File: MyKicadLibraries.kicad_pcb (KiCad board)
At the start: 2 copper layers, 168.6 x 98.9 mm, 27 parts, among them J1 Conn_01x08, J10 RCJ-22, J2 Conn_01x08, J3 POGO Pins, J4 c8-inlet, J5 FTDI, J6 Micro_SD_Card, J7 Conn_01x04, J8 Conn_02x04_Counter_Clockwise, J9 Conn_01x04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

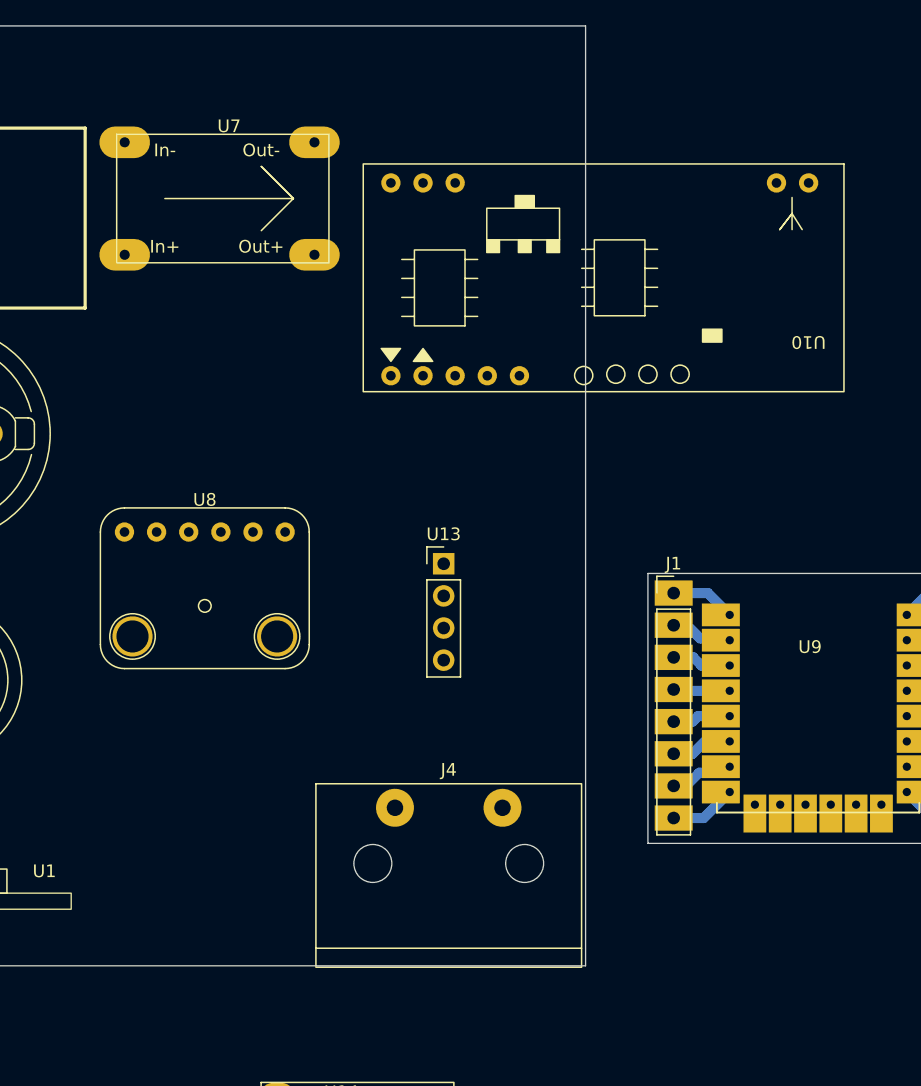
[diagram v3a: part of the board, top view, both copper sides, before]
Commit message: Add midi connector
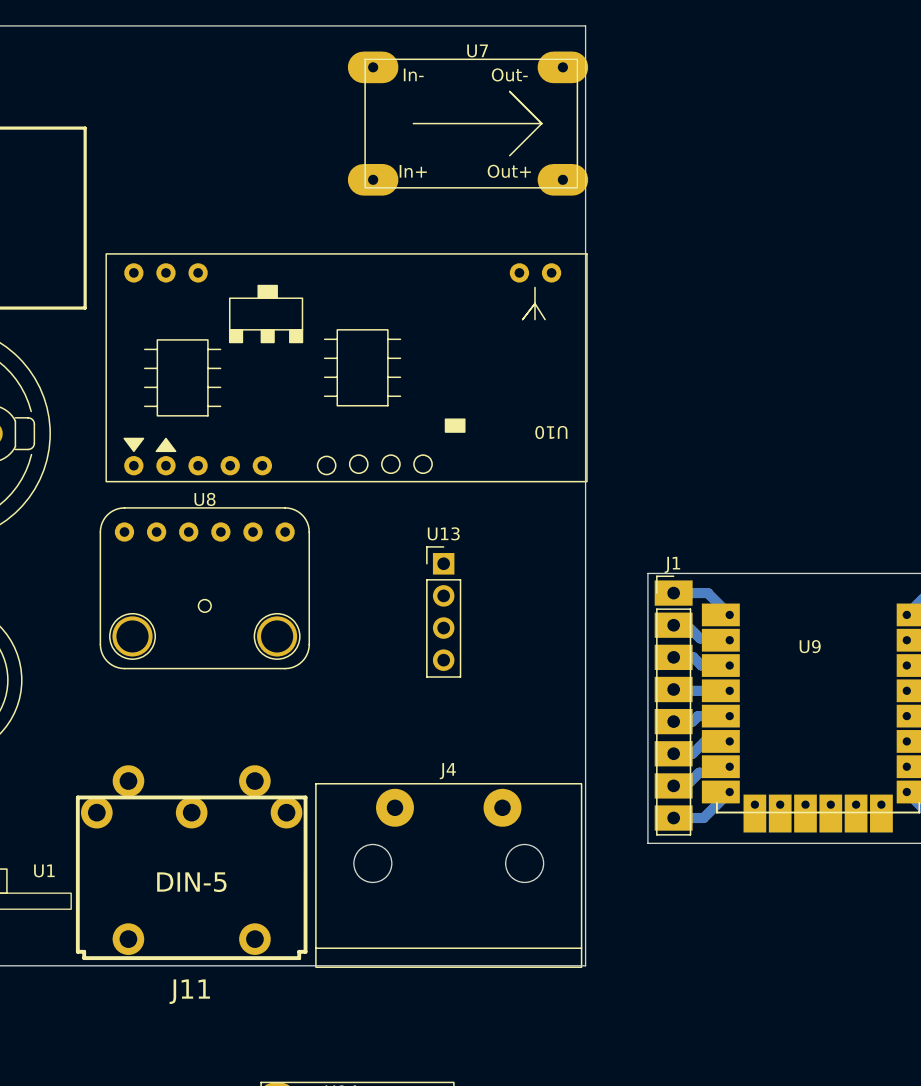
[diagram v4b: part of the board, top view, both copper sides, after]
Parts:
- added J11: DIN-5, midi:midi, F.Cu at (208.3, 89.5)
- moved U10 21.5 mm to (208.8, 51.3)
- moved U7 20.5 mm to (230.9, 32.0)
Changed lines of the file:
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@@
   (net 169 "unconnected-(J10-Pad2)")
   (net 170 "unconnected-(J10-Pad3)")
+  (net 171 "unconnected-(J11-Pad3)")
+  (net 172 "unconnected-(J11-Pad4)")
+  (net 173 "unconnected-(J11-Pad2)")
+  (net 174 "unconnected-(J11-Pad1)")
+  (net 175 "unconnected-(J11-Pad5)")
   (footprint "LilygoSimT7000:LilygoSIM7000G" (layer "F.Cu")
     (at 123.385 65.255)
@@
   )
   (footprint "rdm-6300:rdm-6300" (layer "F.Cu")
-    (at 229.108 44.196 180)
+    (at 208.788 51.308 180)
     (property "Sheetfile" "MyKicadLibraries.kicad_sch")
     (property "Sheetname" "")
@@
       (scale (xyz 0.3937 0.3937 0.3937))
       (rotate (xyz 0 0 0))
+    )
+  )
+  (footprint "midi:midi" (layer "F.Cu")
+    (at 208.28 89.47277)
+    (descr "Din 5 (MIDI), Pro Signal P/N PSG03463")
+    (property "Sheetfile" "MyKicadLibraries.kicad_sch")
+    (property "Sheetname" "")
+    (attr through_hole)
+    (fp_text reference "J11" (at 0 11.00074) (layer "F.SilkS")
+      (effects (font (size 1.524 1.524) (thickness 0.3048)))
+    )
+    (fp_text value "DIN-5" (at 0 2.54) (layer "F.SilkS")
+      (effects (font (size 1.524 1.524) (thickness 0.3048)))
+    )
+    (fp_line (start 8.49884 8.49884) (end -8.49884 8.49884) (layer "F.SilkS") (width 0.3048))
+    (fp_line (start 8.99922 8.001) (end 8.49884 8.001) (layer "F.SilkS") (width 0.3048))
+    (fp_line (start -8.49884 8.001) (end -8.49884 8.49884) (layer "F.SilkS") (width 0.3048))
+    (fp_line (start -9 -4.2) (end -8.99922 8.001) (layer "F.SilkS") (width 0.3048))
+    (fp_line (start -9 -4.2) (end 9 -4.2) (layer "F.SilkS") (width 0.3048))
+    (fp_line (start 8.49884 8.49884) (end 8.49884 8.001) (layer "F.SilkS") (width 0.3048))
+    (fp_line (start -8.99922 8.001) (end -8.49884 8.001) (layer "F.SilkS") (width 0.3048))
+    (fp_line (start 9 -4.2) (end 8.99922 8.001) (layer "F.SilkS") (width 0.3048))
+    (pad "" np_thru_hole circle (at 5.00126 6.9977) (size 2.49936 2.49936) (drill 1.397) (layers *.Cu *.Mask "F.SilkS"))
+    (pad "" np_thru_hole circle (at -5.00126 6.9977) (size 2.49936 2.49936) (drill 1.397) (layers *.Cu *.Mask "F.SilkS"))
+    (pad "1" thru_hole circle (at 7.49808 -2.9972) (size 2.49936 2.49936) (drill 1.397) (layers *.Cu *.SilkS *.Mask)
+      (net 174 "unconnected-(J11-Pad1)") (pintype "passive"))
+    (pad "2" thru_hole circle (at 0 -2.99974) (size 2.49936 2.49936) (drill 1.397) (layers *.Cu *.SilkS *.Mask)
+      (net 173 "unconnected-(J11-Pad2)") (pintype "passive"))
+    (pad "3" thru_hole circle (at -7.49808 -2.9972) (size 2.49936 2.49936) (drill 1.397) (layers *.Cu *.SilkS *.Mask)
+      (net 171 "unconnected-(J11-Pad3)") (pintype "passive"))
+    (pad "4" thru_hole circle (at 4.99618 -5.4991) (size 2.49936 2.49936) (drill 1.397) (layers *.Cu *.SilkS *.Mask)
+      (net 172 "unconnected-(J11-Pad4)") (pintype "passive"))
+    (pad "5" thru_hole circle (at -4.99618 -5.4991) (size 2.49936 2.49936) (drill 1.397) (layers *.Cu *.SilkS *.Mask)
+      (net 175 "unconnected-(J11-Pad5)") (pintype "passive"))
+    (model "${KIPRJMOD}/lib/midi/midi.step"
+      (offset (xyz 0 -9.5 0))
+      (scale (xyz 1 1 1))
+      (rotate (xyz 90 180 -180))
     )
   )
@@
   )
   (footprint "dcdc:dcdc" (layer "F.Cu")
-    (at 211.24 37.93)
-    (property "Sheetfile" "MyKicadLibraries.kicad_sch")
-    (property "Sheetname" "")
+    (at 230.879 32.004)
+    (property "Sheetfile" "MyKicadLibraries.kicad_sch")
+    (property "Sheetname" "")

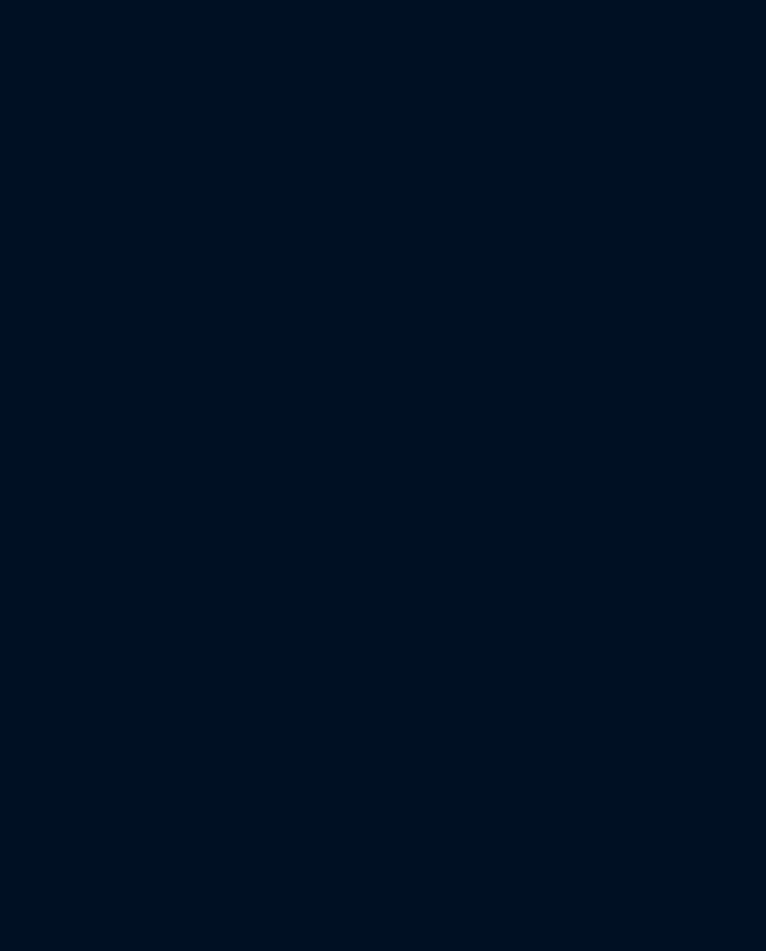
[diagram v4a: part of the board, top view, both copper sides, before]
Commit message: Add din6 midi plug
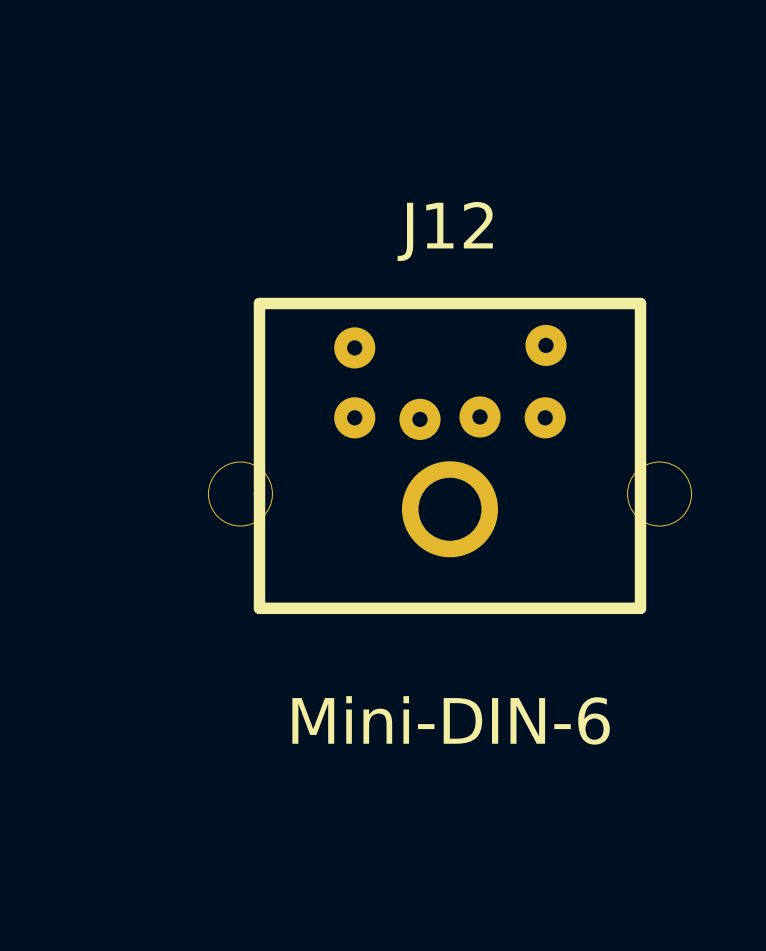
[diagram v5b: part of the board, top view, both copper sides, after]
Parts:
- added J12: Mini-DIN-6, midi:midi-din6, F.Cu at (268.7, 47.8)
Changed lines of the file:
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@@
   (net 174 "unconnected-(J11-Pad1)")
   (net 175 "unconnected-(J11-Pad5)")
+  (net 176 "unconnected-(J12-Pad1)")
+  (net 177 "unconnected-(J12-Pad2)")
+  (net 178 "unconnected-(J12-Pad3)")
+  (net 179 "unconnected-(J12-Pad4)")
+  (net 180 "unconnected-(J12-Pad5)")
+  (net 181 "unconnected-(J12-Pad6)")
+  (footprint "midi:midi-din6" (layer "F.Cu")
+    (at 268.732 47.752)
+    (tags "MINI DIN")
+    (property "Sheetfile" "MyKicadLibraries.kicad_sch")
+    (property "Sheetname" "")
+    (fp_text reference "J12" (at 0 -7.62) (layer "F.SilkS")
+      (effects (font (size 1.524 1.524) (thickness 0.3048)))
+    )
+    (fp_text value "Mini-DIN-6" (at 0 8.89) (layer "F.SilkS")
+      (effects (font (size 1.524 1.524) (thickness 0.3048)))
+    )
+    (fp_line (start -6.35 5.08) (end -6.35 1.27) (layer "F.SilkS") (width 0.381))
+    (fp_line (start 6.35 -5.08) (end 6.35 5.08) (layer "F.SilkS") (width 0.381))
+    (fp_line (start -6.35 -5.08) (end 6.35 -5.08) (layer "F.SilkS") (width 0.381))
+    (fp_line (start -6.35 1.27) (end -6.35 -5.08) (layer "F.SilkS") (width 0.381))
+    (fp_line (start 6.35 5.08) (end -6.35 5.08) (layer "F.SilkS") (width 0.381))
+    (pad "1" thru_hole circle (at 1 -1.3) (size 1.3716 1.3716) (drill 0.508) (layers *.Cu *.Mask "F.SilkS")
+      (net 176 "unconnected-(J12-Pad1)") (pintype "passive"))
+    (pad "2" thru_hole circle (at -1 -1.217) (size 1.3716 1.3716) (drill 0.508) (layers *.Cu *.Mask "F.SilkS")
+      (net 177 "unconnected-(J12-Pad2)") (pintype "passive"))
+    (pad "3" thru_hole circle (at 3.2 -3.683) (size 1.3716 1.3716) (drill 0.508) (layers *.Cu *.Mask "F.SilkS")
+      (net 178 "unconnected-(J12-Pad3)") (pintype "passive"))
+    (pad "4" thru_hole circle (at -3.175 -3.6) (size 1.3716 1.3716) (drill 0.508) (layers *.Cu *.Mask "F.SilkS")
+      (net 179 "unconnected-(J12-Pad4)") (pintype "passive"))
+    (pad "5" thru_hole circle (at 3.175 -1.27) (size 1.3716 1.3716) (drill 0.508) (layers *.Cu *.Mask "F.SilkS")
+      (net 180 "unconnected-(J12-Pad5)") (pintype "passive"))
+    (pad "6" thru_hole circle (at -3.175 -1.27) (size 1.3716 1.3716) (drill 0.508) (layers *.Cu *.Mask "F.SilkS")
+      (net 181 "unconnected-(J12-Pad6)") (pintype "passive"))
+    (pad "GND" thru_hole circle (at -6.985 1.27) (size 2.16916 2.16916) (drill 2.1) (layers *.Cu *.SilkS *.Mask))
+    (pad "GND" thru_hole circle (at 6.985 1.27) (size 2.16916 2.16916) (drill 2.1) (layers *.Cu *.SilkS *.Mask))
+    (pad "GND" thru_hole circle (at 0 1.778) (size 3.2004 3.2004) (drill 2.1) (layers *.Cu *.SilkS *.Mask))
+    (model "/Users/besi/Dropbox/projects/MyKicadLibraries/lib/midi/minidin_6.wrl"
+      (offset (xyz 0 0 0))
+      (scale (xyz 1 1 1))
+      (rotate (xyz 0 0 0))
+    )
+  )
   (footprint "LilygoSimT7000:LilygoSIM7000G" (layer "F.Cu")
     (at 123.385 65.255)

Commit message: Update submodules
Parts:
- added U15: esp32-wemos-d1-mini, esp32-wemos-d1-mini:esp32-wemos-d1-mini, F.Cu at (118.1, 138.4)
- added U16: TCRT5000, tcrt5000:tcrt5000, F.Cu at (110.5, 29.2)
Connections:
- U12 pad 3: Net-(U12-Pad11) -> unconnected-(U12-Pad3)
- U12 pad 5: (no net) -> unconnected-(U12-Pad5)
- U12 pad 6: (no net) -> unconnected-(U12-Pad6)
- U12 pad 7: Net-(U12-Pad7) -> unconnected-(U12-Pad7)
- U12 pad 8: Net-(U12-Pad7) -> unconnected-(U12-Pad8)

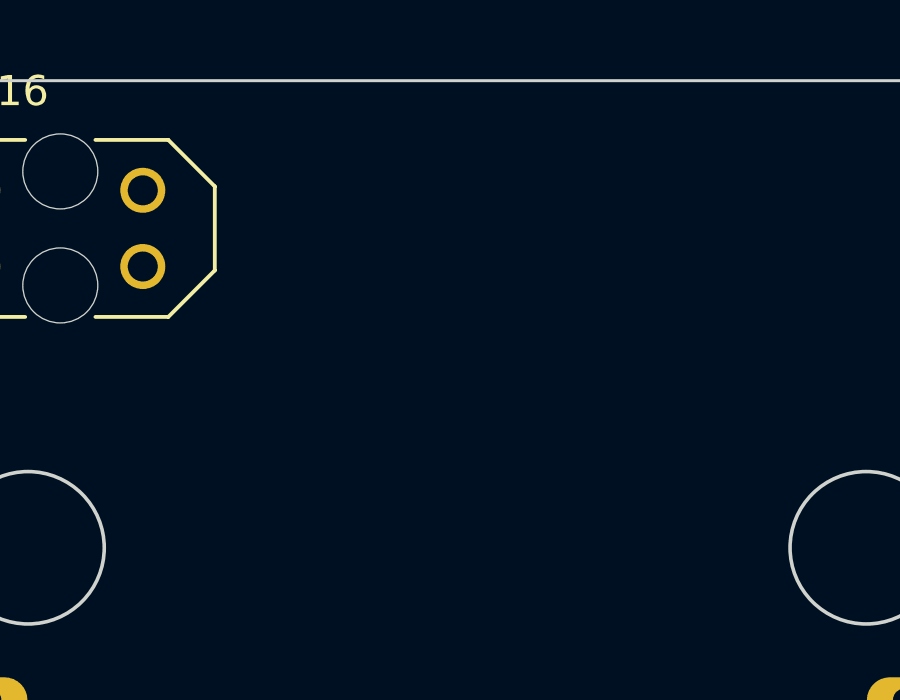
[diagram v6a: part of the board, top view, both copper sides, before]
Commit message: Add USB pcb trace footprint
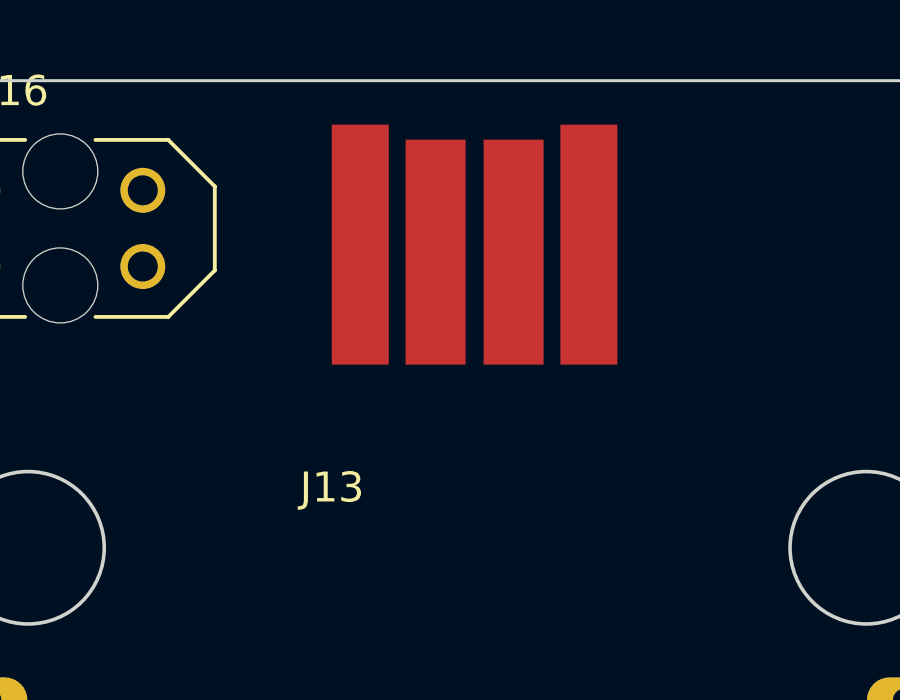
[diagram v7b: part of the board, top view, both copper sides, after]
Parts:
- added J13: USB_A, usb-a-pcb:usb-a-pcb, F.Cu at (118.3, 36.9)
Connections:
- U16 pad CATH: (no net) -> unconnected-(U16-PadCATH)
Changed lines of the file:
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@@
   (net 226 "unconnected-(U16-PadCOLL)")
   (net 227 "unconnected-(U16-PadE)")
+  (net 228 "unconnected-(U16-PadCATH)")
+  (net 229 "unconnected-(J13-Pad1)")
+  (net 230 "unconnected-(J13-Pad2)")
+  (net 231 "unconnected-(J13-Pad3)")
+  (net 232 "unconnected-(J13-Pad4)")
   (footprint "esp32-wemos-d1-mini:esp32-wemos-d1-mini" (layer "F.Cu")
     (at 118.11 138.43)
@@
       (net 225 "unconnected-(U16-PadA)") (pintype "passive") (solder_mask_margin 0.102))
     (pad "CATH" thru_hole circle (at 2.75 1.27) (size 1.5 1.5) (drill 1) (layers *.Cu *.Mask)
-      (solder_mask_margin 0.102))
+      (net 228 "unconnected-(U16-PadCATH)") (pintype "passive") (solder_mask_margin 0.102))
     (pad "COLL" thru_hole circle (at -2.75 -1.27) (size 1.5 1.5) (drill 1) (layers *.Cu *.Mask)
       (net 226 "unconnected-(U16-PadCOLL)") (pintype "passive") (solder_mask_margin 0.102))
@@
     )
   )
+  (footprint "usb-a-pcb:usb-a-pcb" (layer "F.Cu")
+    (at 118.3 36.85)
+    (property "Sheetfile" "MyKicadLibraries.kicad_sch")
+    (property "Sheetname" "")
+    (attr exclude_from_pos_files)
+    (fp_text reference "J13" (at 0.13 -7.85) (layer "F.SilkS") hide
+      (effects (font (size 1.5 1.5) (thickness 0.15)))
+    )
+    (fp_text value "USB_A" (at 0.29 -10.13) (layer "F.Fab") hide
+      (effects (font (size 1.016 1.016) (thickness 0.2032)))
+    )
+    (fp_text user "${REFERENCE}" (at 1.25 1 180) (layer "F.SilkS")
+      (effects (font (size 1 1) (thickness 0.15)))
+    )
+    (fp_text user "${REFERENCE}" (at 6 -5.75 180) (layer "F.Fab")
+      (effects (font (size 1 1) (thickness 0.15)))
+    )
+    (fp_line (start 3.5 0) (end 3 0) (layer "F.Fab") (width 0.04064))
+    (fp_line (start 2.5 0) (end 2 0) (layer "F.Fab") (width 0.04064))
+    (fp_line (start 0 0) (end 0 -12) (layer "F.Fab") (width 0.04064))
+    (fp_line (start 5.5 0) (end 5 0) (layer "F.Fab") (width 0.04064))
+    (fp_line (start 8.5 0) (end 8 0) (layer "F.Fab") (width 0.04064))
+    (fp_line (start 12 0) (end 11 0) (layer "F.Fab") (width 0.04064))
+    (fp_line (start 7.5 0) (end 7 0) (layer "F.Fab") (width 0.04064))
+    (fp_line (start 9.5 0) (end 9 0) (layer "F.Fab") (width 0.04064))
+    (fp_line (start 6.5 0) (end 6 0) (layer "F.Fab") (width 0.04064))
+    (fp_line (start 4.5 0) (end 4 0) (layer "F.Fab") (width 0.04064))
+    (fp_line (start 0.5 0) (end 0 0) (layer "F.Fab") (width 0.04064))
+    (fp_line (start 10.5 0) (end 10 0) (layer "F.Fab") (width 0.04064))
+    (fp_line (start 12 -12) (end 12 0) (layer "F.Fab") (width 0.04064))
+    (fp_line (start 1.5 0) (end 1 0) (layer "F.Fab") (width 0.04064))
+    (fp_line (start 0 -12) (end 12 -12) (layer "F.Fab") (width 0.04064))
+    (pad "1" connect rect (at 2.19 -7.1 180) (size 1.9 8) (layers "F.Cu" "F.Mask")
+      (net 229 "unconnected-(J13-Pad1)") (pinfunction "VBUS") (pintype "power_in"))
+    (pad "2" connect rect (at 4.7 -6.85 180) (size 2 7.5) (layers "F.Cu" "F.Mask")
+      (net 230 "unconnected-(J13-Pad2)") (pinfunction "D-") (pintype "bidirectional"))
+    (pad "3" connect rect (at 7.3 -6.85 180) (size 2 7.5) (layers "F.Cu" "F.Mask")
+      (net 231 "unconnected-(J13-Pad3)") (pinfunction "D+") (pintype "bidirectional"))
+    (pad "4" connect rect (at 9.81 -7.1 180) (size 1.9 8) (layers "F.Cu" "F.Mask")
+      (net 232 "unconnected-(J13-Pad4)") (pinfunction "GND") (pintype "power_in"))
+  )
   (footprint "Connector_PinHeader_2.54mm:PinHeader_1x04_P2.54mm_Vertical" (layer "F.Cu")
